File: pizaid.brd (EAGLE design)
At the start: 65 x 56 mm, 35 parts, among them X1 DCJACK-MJ179P-R

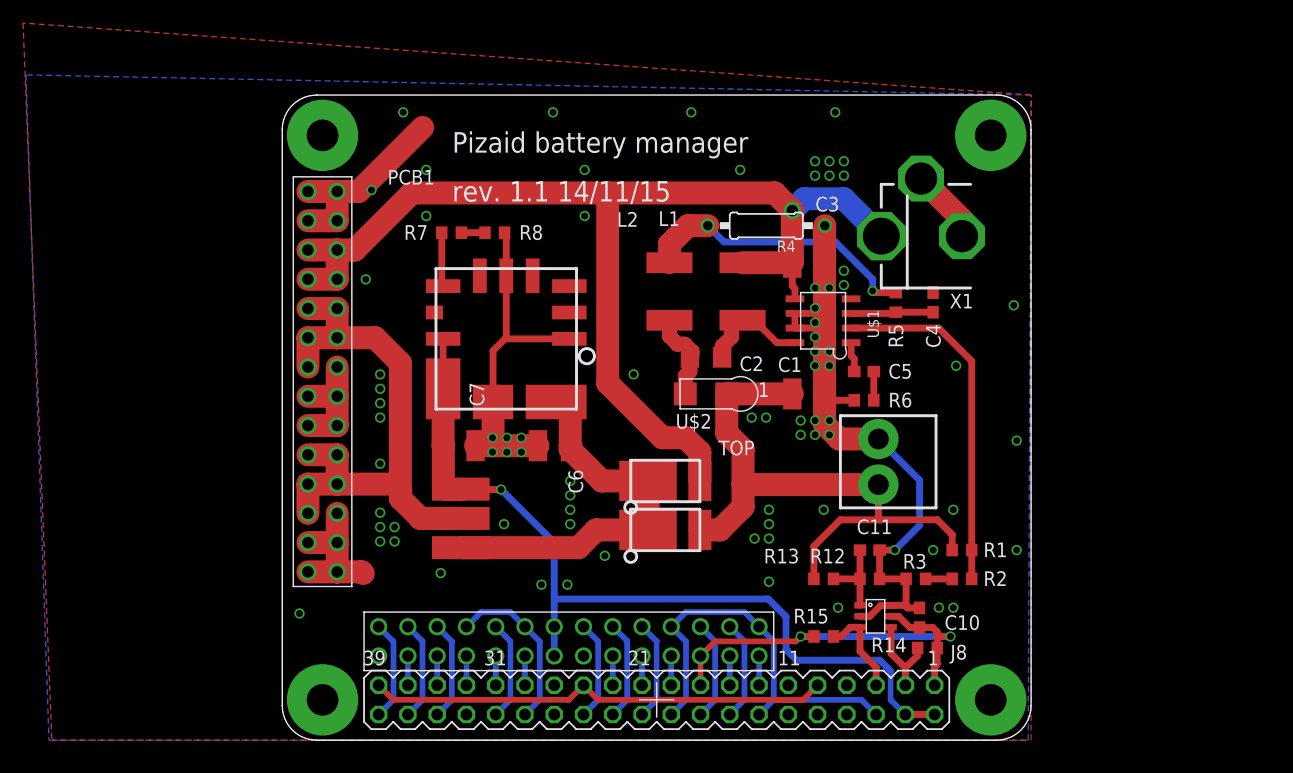
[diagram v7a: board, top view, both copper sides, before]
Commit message: add default output jumper to 5V
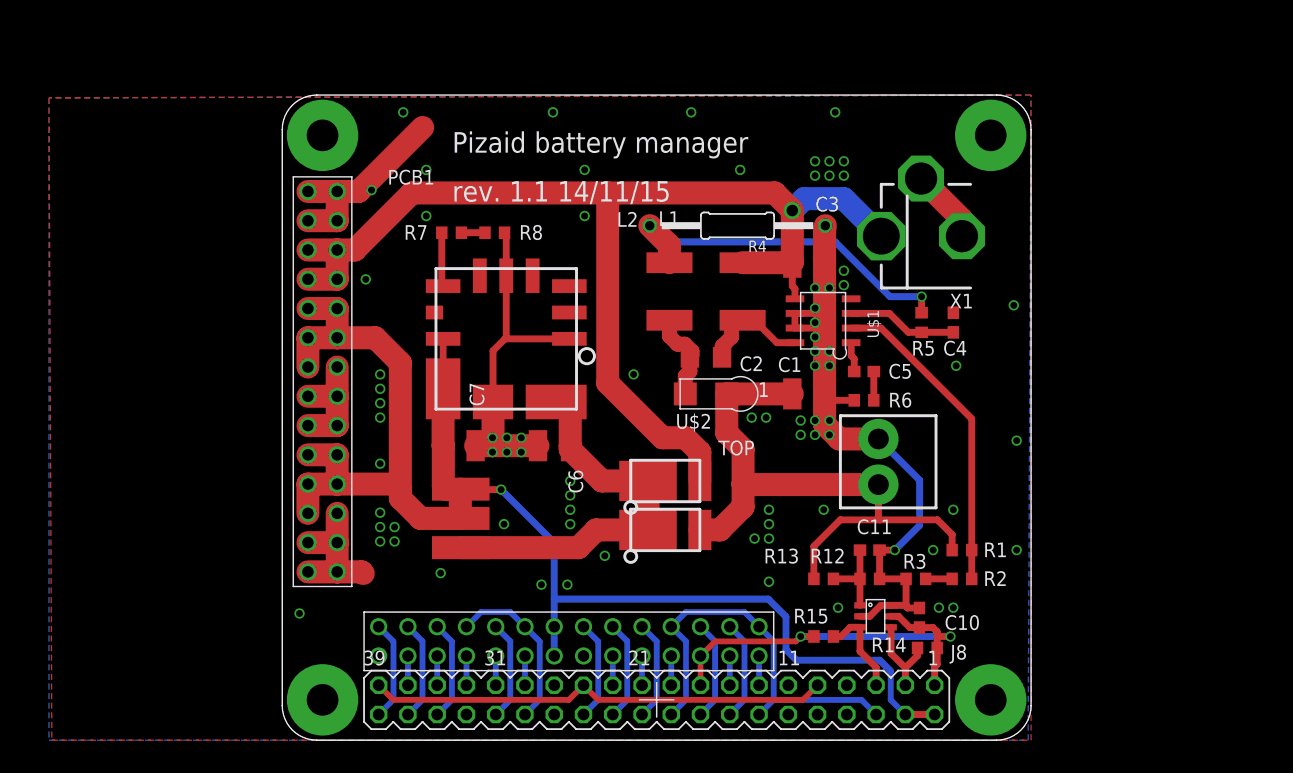
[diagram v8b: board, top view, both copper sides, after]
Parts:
- R4: device rcl:0207/10 -> rcl:0207/15
- moved R5 2.85 mm to (80.5, 40.2)
- moved R4 2.50 mm to (64.5, 48.7)
- moved C4 2.47 mm to (83.2, 40.2)
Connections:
- removed net N$30: U$11.P$2, U$3.P$10, U$3.P$11, U$3.P$12, U$3.P$13, U$3.P$19, U$3.P$20, U$3.P$21, U$3.P$22, U$3.P$23, U$3.P$9
- net 5V0@2: now also U$11.P$2, U$3.P$10, U$3.P$11, U$3.P$12, U$3.P$13, U$3.P$19, U$3.P$20, U$3.P$21, U$3.P$22, U$3.P$23, U$3.P$9
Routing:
- net 5V0@2: track 74.6 -> 127.3 mm
- net N$30: track 50.1 -> 0.00 mm
- net N$4: track 24.9 -> 31.5 mm
- net N$10: track 30.6 -> 27.6 mm
- net N$5: track 7.27 -> 9.55 mm
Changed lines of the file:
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@@
 <attribute name="VALUE" x="78.865" y="21.345" size="1.27" layer="27"/>
 </element>
-<element name="R4" library="rcl" package="0207/10" value="0.2" x="67.02" y="48.6625" smashed="yes" rot="R180">
-<attribute name="NAME" x="69.56" y="47.3671" size="0.9906" layer="25" ratio="10" rot="R180"/>
-<attribute name="VALUE" x="65.8544" y="50.1049" size="0.9906" layer="27" ratio="10"/>
-</element>
-<element name="R5" library="rcl" package="R0603" value="24" x="78.25" y="42" smashed="yes" rot="R270">
-<attribute name="NAME" x="77.635" y="40.135" size="1.27" layer="25" rot="R270"/>
-<attribute name="VALUE" x="74.865" y="43.845" size="1.27" layer="27"/>
+<element name="R4" library="rcl" package="0207/15" value="0.2" x="64.52" y="48.6625" smashed="yes" rot="R180">
+<attribute name="NAME" x="67.06" y="47.3671" size="0.9906" layer="25" ratio="10" rot="R180"/>
+<attribute name="VALUE" x="63.3544" y="50.1049" size="0.9906" layer="27" ratio="10"/>
+</element>
+<element name="R5" library="rcl" package="R0603" value="24" x="80.5" y="40.25" smashed="yes" rot="R270">
+<attribute name="NAME" x="79.615" y="37.385" size="1.27" layer="25"/>
+<attribute name="VALUE" x="77.115" y="42.095" size="1.27" layer="27"/>
 </element>
 <element name="R6" library="rcl" package="R0603" value="1k" x="75.5" y="33.5" smashed="yes" rot="R180">
@@
 <attribute name="VALUE" x="71.77" y="52.0625" size="1.27" layer="27"/>
 </element>
-<element name="C4" library="rcl" package="C0603" value="0.22u" x="81.5" y="42" smashed="yes" rot="R90">
-<attribute name="NAME" x="80.885" y="40.135" size="1.27" layer="25" rot="R270"/>
-<attribute name="VALUE" x="82.155" y="33.365" size="1.27" layer="27" rot="R90"/>
+<element name="C4" library="rcl" package="C0603" value="0.22u" x="83.25" y="40.25" smashed="yes" rot="R90">
+<attribute name="NAME" x="82.365" y="37.385" size="1.27" layer="25"/>
+<attribute name="VALUE" x="85.115" y="37.345" size="1.27" layer="27"/>
 </element>
 <element name="C5" library="rcl" package="C0603" value="0.1u" x="75.5" y="36" smashed="yes">
 <attribute name="NAME" x="77.615" y="35.385" size="1.27" layer="25"/>
-<attribute name="VALUE" x="76.365" y="37.345" size="1.27" layer="27"/>
+<attribute name="VALUE" x="80.615" y="35.345" size="1.27" layer="27"/>
 </element>
 <element name="L1" library="rcl" package="L5650M" value="33u" x="64.96" y="42.9475" smashed="yes" rot="R270">
@@
 <contactref element="U$10" pad="P$2"/>
 <wire x1="72.075" y1="45.4875" x2="72.075" y2="48.1575" width="2" layer="1"/>
-<wire x1="72.075" y1="48.1575" x2="72.1" y2="48.6625" width="2" layer="1"/>
+<wire x1="72.075" y1="48.1575" x2="72.14" y2="48.6625" width="2" layer="1"/>
 <wire x1="72.075" y1="45.4875" x2="72.075" y2="41.1875" width="2" layer="1"/>
 <wire x1="72.075" y1="41.1875" x2="72.075" y2="35.5625" width="2" layer="1"/>
@@
 <wire x1="69.505" y1="39.7725" x2="69.505" y2="41.0425" width="0.6" layer="1"/>
 <polygon width="0.4" layer="1" isolate="0.3" thermals="no">
-<vertex x="2.5" y="66.25"/>
+<vertex x="4.75" y="59.75"/>
 <vertex x="5" y="4"/>
 <vertex x="90" y="4"/>
@@
 <wire x1="80.325" y1="26.57" x2="76.75" y2="30.145" width="0.6" layer="16"/>
 <polygon width="0.4" layer="16" isolate="0.3" thermals="no">
-<vertex x="2.75" y="61.75"/>
+<vertex x="4.75" y="59.75"/>
 <vertex x="4.75" y="4"/>
 <vertex x="89.75" y="4"/>
@@
 <contactref element="R4" pad="2"/>
 <contactref element="R5" pad="1"/>
-<wire x1="58.61" y1="45.4475" x2="58.61" y2="47.0475" width="2" layer="1"/>
-<wire x1="58.61" y1="47.0475" x2="60.225" y2="48.6625" width="2" layer="1"/>
-<wire x1="61.94" y1="48.6625" x2="60.225" y2="48.6625" width="2" layer="1"/>
-<wire x1="61.94" y1="48.6625" x2="63.3525" y2="47.25" width="0.6" layer="16"/>
-<wire x1="63.3525" y1="47.25" x2="73" y2="47.25" width="0.6" layer="16"/>
-<wire x1="73" y1="47.25" x2="76.25" y2="44" width="0.6" layer="16"/>
-<wire x1="76.25" y1="44" x2="76.25" y2="43" width="0.6" layer="16"/>
-<via x="76.25" y="43" extent="1-16" drill="0.6"/>
-<wire x1="76.25" y1="43" x2="76.4" y2="42.85" width="0.6" layer="1"/>
-<wire x1="76.4" y1="42.85" x2="78.25" y2="42.85" width="0.6" layer="1"/>
+<wire x1="58.3125" y1="47.25" x2="73" y2="47.25" width="0.6" layer="16"/>
+<wire x1="73" y1="47.25" x2="77.75" y2="42.5" width="0.6" layer="16"/>
+<wire x1="58.61" y1="45.4475" x2="58.61" y2="46.9525" width="2" layer="1"/>
+<wire x1="58.61" y1="46.9525" x2="56.9" y2="48.6625" width="2" layer="1"/>
+<wire x1="58.3125" y1="47.25" x2="56.9" y2="48.6625" width="0.6" layer="16"/>
+<wire x1="77.75" y1="42.5" x2="80.5" y2="42.5" width="0.6" layer="16"/>
+<via x="80.5" y="42.5" extent="1-16" drill="0.6"/>
+<wire x1="80.5" y1="42.5" x2="80.5" y2="41.1" width="0.6" layer="1"/>
 </signal>
 <signal name="N$5">
@@
 <contactref element="U$1" pad="3"/>
 <contactref element="C4" pad="1"/>
-<wire x1="78.25" y1="41.0425" x2="78.25" y2="41.15" width="0.5" layer="1"/>
-<wire x1="74.385" y1="41.0425" x2="78.1425" y2="41.0425" width="0.6" layer="1"/>
-<wire x1="78.1425" y1="41.0425" x2="78.25" y2="41.15" width="0.6" layer="1"/>
-<wire x1="81.5" y1="41.15" x2="78.25" y2="41.15" width="0.6" layer="1"/>
+<wire x1="74.385" y1="41.0425" x2="77.7075" y2="41.0425" width="0.6" layer="1"/>
+<wire x1="80.5" y1="39.4" x2="83.25" y2="39.4" width="0.6" layer="1"/>
+<wire x1="77.7075" y1="41.0425" x2="79.35" y2="39.4" width="0.6" layer="1"/>
+<wire x1="80.5" y1="39.4" x2="79.35" y2="39.4" width="0.6" layer="1"/>
 </signal>
 <signal name="N$6">
@@
 <contactref element="R1" pad="1"/>
 <wire x1="84.85" y1="18" x2="84.85" y2="20.5" width="0.6" layer="1"/>
-<wire x1="74.385" y1="39.7725" x2="81.9775" y2="39.7725" width="0.6" layer="1"/>
-<wire x1="81.9775" y1="39.7725" x2="84.85" y2="36.9" width="0.6" layer="1"/>
-<wire x1="84.85" y1="20.5" x2="84.85" y2="36.9" width="0.6" layer="1"/>
+<wire x1="81.9775" y1="39.7725" x2="84.85" y2="36.9" width="0" layer="19" extent="1-16"/>
+<wire x1="84.85" y1="20.5" x2="84.85" y2="31.9" width="0.6" layer="1"/>
+<wire x1="84.85" y1="30.4" x2="84.85" y2="36.9" width="0" layer="19" extent="1-16"/>
+<wire x1="74.385" y1="39.7725" x2="76.9775" y2="39.7725" width="0.6" layer="1"/>
+<wire x1="76.9775" y1="39.7725" x2="84.85" y2="31.9" width="0.6" layer="1"/>
+<wire x1="84.85" y1="31.9" x2="84.85" y2="30.4" width="0" layer="19" extent="1-16"/>
 </signal>
 <signal name="N$11">
@@
 <wire x1="40.54" y1="25.75" x2="40.5" y2="25.79" width="0.6" layer="1"/>
 <wire x1="38.9625" y1="34.5" x2="38.9625" y2="38.835" width="0.6" layer="1"/>
+<contactref element="U$3" pad="P$9"/>
+<contactref element="U$3" pad="P$11"/>
+<contactref element="U$3" pad="P$13"/>
+<contactref element="U$3" pad="P$19"/>
+<contactref element="U$3" pad="P$21"/>
+<contactref element="U$3" pad="P$23"/>
+<contactref element="U$3" pad="P$20"/>
+<contactref element="U$3" pad="P$22"/>
+<contactref element="U$3" pad="P$12"/>
+<contactref element="U$3" pad="P$10"/>
+<contactref element="U$11" pad="P$2"/>
+<wire x1="27.23" y1="36.39" x2="27.23" y2="38.93" width="2" layer="1"/>
+<wire x1="27.23" y1="28.77" x2="29.77" y2="28.77" width="2" layer="1"/>
+<wire x1="27.23" y1="26.23" x2="29.77" y2="26.23" width="2" layer="1"/>
+<wire x1="29.77" y1="26.23" x2="29.77" y2="28.77" width="2" layer="1"/>
+<wire x1="27.23" y1="26.23" x2="27.23" y2="23.69" width="2" layer="1"/>
+<wire x1="29.77" y1="41.47" x2="29.77" y2="38.93" width="2" layer="1"/>
+<wire x1="27.23" y1="41.47" x2="29.77" y2="41.47" width="2" layer="1"/>
+<wire x1="27.23" y1="38.93" x2="29.77" y2="38.93" width="2" layer="1"/>
+<wire x1="40.5" y1="23.25" x2="37" y2="23.25" width="2" layer="1"/>
+<wire x1="37" y1="23.25" x2="35.25" y2="25" width="2" layer="1"/>
+<wire x1="35.25" y1="25" x2="35.25" y2="25.75" width="2" layer="1"/>
+<wire x1="35.25" y1="25.75" x2="35.25" y2="36.75" width="2" layer="1"/>
+<wire x1="35.25" y1="36.75" x2="33.07" y2="38.93" width="2" layer="1"/>
+<wire x1="29.77" y1="38.93" x2="33.07" y2="38.93" width="2" layer="1"/>
+<wire x1="29.77" y1="26.23" x2="34.77" y2="26.23" width="2" layer="1"/>
+<wire x1="34.77" y1="26.23" x2="35.25" y2="25.75" width="2" layer="1"/>
+<wire x1="40.46" y1="25.75" x2="40.46" y2="23.29" width="2" layer="1"/>
+<wire x1="40.46" y1="23.29" x2="40.5" y2="23.25" width="2" layer="1"/>
 </signal>
 <signal name="N$9">
@@
 <wire x1="49.895" y1="33.355" x2="48.7775" y2="33.355" width="2" layer="1"/>
 </signal>
-<signal name="N$30">
-<contactref element="U$3" pad="P$9"/>
-<contactref element="U$3" pad="P$11"/>
-<contactref element="U$3" pad="P$13"/>
-<wire x1="27.23" y1="36.39" x2="27.23" y2="38.93" width="2" layer="1"/>
-<contactref element="U$3" pad="P$19"/>
-<contactref element="U$3" pad="P$21"/>
-<contactref element="U$3" pad="P$23"/>
-<contactref element="U$3" pad="P$20"/>
-<contactref element="U$3" pad="P$22"/>
-<wire x1="27.23" y1="28.77" x2="29.77" y2="28.77" width="2" layer="1"/>
-<wire x1="27.23" y1="26.23" x2="29.77" y2="26.23" width="2" layer="1"/>
-<wire x1="29.77" y1="26.23" x2="29.77" y2="28.77" width="2" layer="1"/>
-<wire x1="27.23" y1="26.23" x2="27.23" y2="23.69" width="2" layer="1"/>
-<contactref element="U$3" pad="P$12"/>
-<contactref element="U$3" pad="P$10"/>
-<wire x1="29.77" y1="41.47" x2="29.77" y2="38.93" width="2" layer="1"/>
-<contactref element="U$11" pad="P$2"/>
-<wire x1="27.23" y1="41.47" x2="29.77" y2="41.47" width="2" layer="1"/>
-<wire x1="27.23" y1="38.93" x2="29.77" y2="38.93" width="2" layer="1"/>
-<wire x1="40.5" y1="23.25" x2="37" y2="23.25" width="2" layer="1"/>
-<wire x1="37" y1="23.25" x2="35.25" y2="25" width="2" layer="1"/>
-<wire x1="35.25" y1="25" x2="35.25" y2="25.75" width="2" layer="1"/>
-<wire x1="35.25" y1="25.75" x2="35.25" y2="36.75" width="2" layer="1"/>
-<wire x1="35.25" y1="36.75" x2="33.07" y2="38.93" width="2" layer="1"/>
-<wire x1="29.77" y1="38.93" x2="33.07" y2="38.93" width="2" layer="1"/>
-<wire x1="29.77" y1="26.23" x2="34.77" y2="26.23" width="2" layer="1"/>
-<wire x1="34.77" y1="26.23" x2="35.25" y2="25.75" width="2" layer="1"/>
-</signal>
 </signals>
